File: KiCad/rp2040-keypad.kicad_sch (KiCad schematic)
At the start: 21 parts

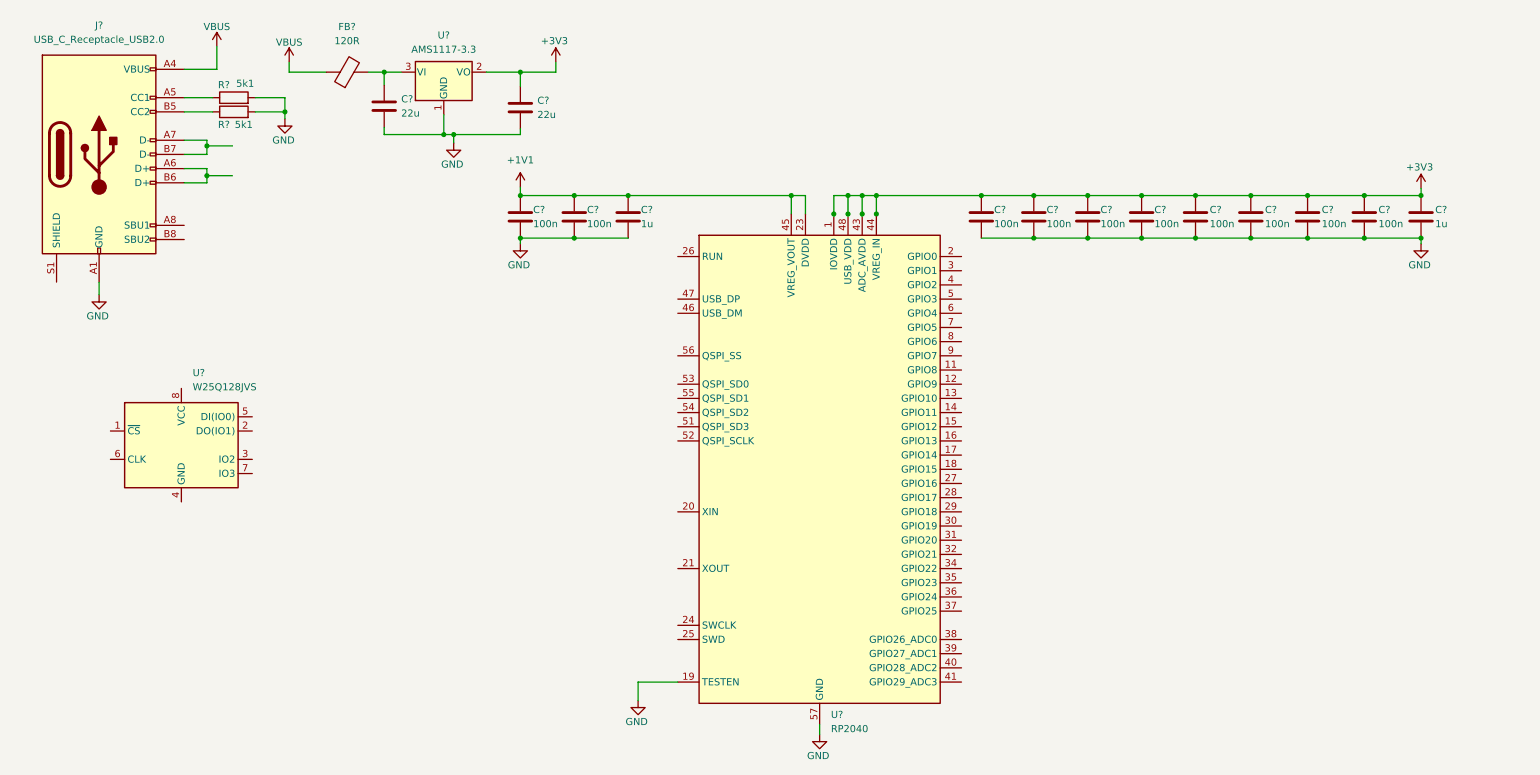
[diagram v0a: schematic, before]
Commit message: Finish schematic and footprint assignment
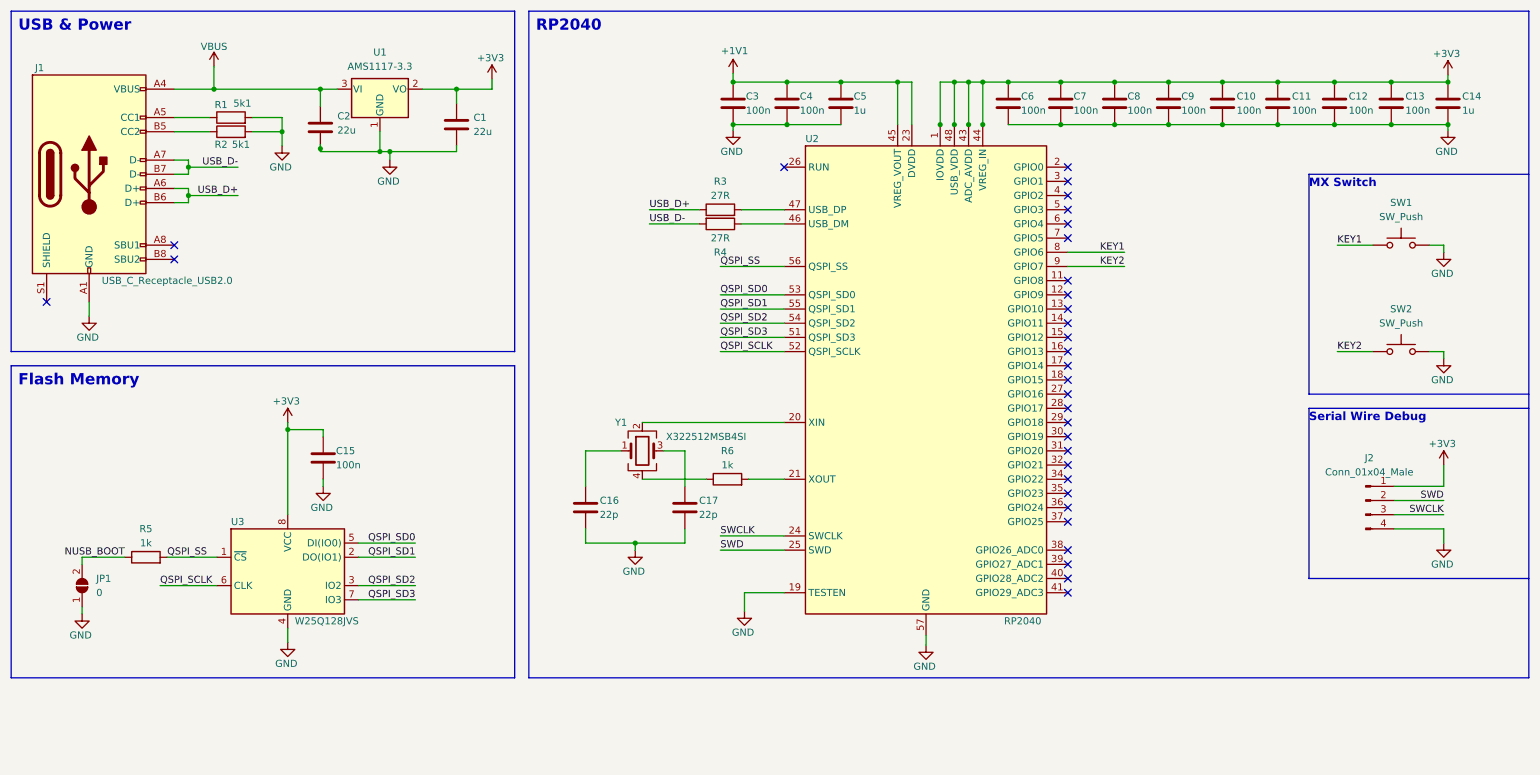
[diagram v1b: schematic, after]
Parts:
- removed FB?: 120R, symbol Device:FerriteBead
- added C15: 100n, Capacitor_SMD:C_0402_1005Metric, symbol Device:C
- added C16, C17: 22p, Capacitor_SMD:C_0402_1005Metric, symbol Device:C
- added J2: Conn_01x04_Male, Connector_Wire:SolderWire-0.1sqmm_1x04_P3.6mm_D0.4mm_OD1mm, symbol Connector:Conn_01x04_Male
- added JP1: 0, Jumper:SolderJumper-2_P1.3mm_Open_Pad1.0x1.5mm, symbol Jumper:SolderJumper_2_Open
- added R3, R4: 27R, Resistor_SMD:R_0402_1005Metric, symbol Device:R
- added R5, R6: 1k, Resistor_SMD:R_0402_1005Metric, symbol Device:R
- added SW1, SW2: SW_Push, Switch_Keyboard_Cherry_MX:SW_Cherry_MX_PCB_1.00u, symbol Switch:SW_Push
- added Y1: X322512MSB4SI, Crystal:Crystal_SMD_3225-4Pin_3.2x2.5mm, symbol Device:Crystal_GND24
- C1, C2: renamed from C?; footprint (none) -> Capacitor_SMD:C_0603_1608Metric
- C10, C11, C12, C13, C14, C3, C4, C5, C6, C7, C8, C9: renamed from C?; footprint (none) -> Capacitor_SMD:C_0402_1005Metric
- J1: renamed from J?; footprint (none) -> Connector_USB:USB_C_Receptacle_HRO_TYPE-C-31-M-12
- R1, R2: renamed from R?; footprint (none) -> Resistor_SMD:R_0402_1005Metric
- gave numbers to parts that had none: 3
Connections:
- net +3V3: now also U3.8 (VCC), C15.1, J2.1 (Pin_1)
- net GND: now also U3.4 (GND), C15.2, C16.2, C17.2, J2.4 (Pin_4), JP1.1 (A), SW1.2, SW2.2
- net VBUS: now also C2.1, U1.3 (VI)
- net at U2.20 (XIN): now also Y1.2
- net at U2.21 (XOUT): now also R6.2
- net SWCLK: now reaches U2.24 (SWCLK)
- net SWCLK: now also J2.3 (Pin_3)
- net SWD: now reaches U2.25 (SWD)
- net SWD: now also J2.2 (Pin_2)
- net at U2.46 (USB_DM): now also R4.1
- net at U2.47 (USB_DP): now also R3.2
- net QSPI_SD3: now reaches U2.51 (QSPI_SD3)
- net QSPI_SD3: now also U3.7 (IO3)
- net QSPI_SCLK: now reaches U2.52 (QSPI_SCLK)
- net QSPI_SCLK: now also U3.6 (CLK)
- net QSPI_SD0: now reaches U2.53 (QSPI_SD0)
- net QSPI_SD0: now also U3.5 (DI(IO0))
- net QSPI_SD2: now reaches U2.54 (QSPI_SD2)
- net QSPI_SD2: now also U3.3 (IO2)
- net QSPI_SD1: now reaches U2.55 (QSPI_SD1)
- net QSPI_SD1: now also U3.2 (DO(IO1))
- net QSPI_SS: now reaches U2.56 (QSPI_SS)
- net QSPI_SS: now also U3.1 (~{CS}), R5.2
- net KEY1: now reaches U2.8 (GPIO6)
- net KEY1: now also SW1.1
- net KEY2: now reaches U2.9 (GPIO7)
- net KEY2: now also SW2.1
- net USB_D+: now reaches J1.A6 (D+), J1.B6 (D+)
- net USB_D+: now also R3.1
- net USB_D-: now reaches J1.A7 (D-), J1.B7 (D-)
- net USB_D-: now also R4.2
- new net: C16.1, Y1.1
- new net: C17.1, Y1.3
- new net: R6.1, Y1.4
- new net NUSB_BOOT: JP1.2 (B), R5.1
- no-connect marks 0 -> 32
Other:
- note added: "Flash Memory"
- note added: "MX Switch"
- note added: "RP2040"
- note added: "Serial Wire Debug"
- note added: "USB & Power"
- moved on the sheet: C1, C10, C11, C12, C13, C14, C2, C3, C4, C5, C6, C7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

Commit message: First draft completed ready to review
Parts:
- added H1, H2, H3, H4: MountingHole, MountingHole:MountingHole_2.2mm_M2_DIN965, symbol Mechanical:MountingHole
- C1, C2: LCSC (none) -> C59461
- C10, C11, C12, C13, C15, C3, C4, C6, C7, C8, C9: LCSC (none) -> C1525
- C14, C5: LCSC (none) -> C52923
- C16, C17: LCSC (none) -> C1555
- J1: LCSC (none) -> C165948
- R1, R2: LCSC (none) -> C25905
- R3, R4: value 27R -> 27R4; LCSC (none) -> C26971
- R5, R6: LCSC (none) -> C11702
- U1: LCSC (none) -> C6186
- U2: LCSC (none) -> C2040
- U3: LCSC (none) -> C97521
- Y1: value X322512MSB4SI -> 12Mhz; LCSC (none) -> C9002
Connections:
- net GND: now also Y1.2, Y1.4
- net at Y1.1: now also C17.1, R6.1; no longer C16.1
- net at U2.20 (XIN): now also C16.1, Y1.3; no longer Y1.2
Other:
- moved on the sheet: Y1

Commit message: Rev 0.1 ready for production
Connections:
- net D-: now reaches R4.1, U2.46 (USB_DM)
- net D+: now reaches R3.2, U2.47 (USB_DP)
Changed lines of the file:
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@@
     (effects (font (size 1.27 1.27)) (justify right bottom))
+  )
+  (label "D+" (at 147.32 48.26 0)
+    (effects (font (size 1.27 1.27)) (justify left bottom))
   )
   (label "SWD" (at 269.24 100.33 180)
@@
     (effects (font (size 1.27 1.27)) (justify left bottom))
   )
+  (label "D-" (at 147.32 50.8 0)
+    (effects (font (size 1.27 1.27)) (justify left bottom))
+  )

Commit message: Fix component ID R3&R4 for JLCPCB
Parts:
- R3, R4: LCSC C26971 -> C31439
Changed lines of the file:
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@@
       (effects (font (size 1.27 1.27)) hide)
     )
-    (property "LCSC" "C26971" (id 4) (at 139.7 50.8 90)
+    (property "LCSC" "C31439" (id 4) (at 139.7 50.8 90)
       (effects (font (size 1.27 1.27)) hide)
     )
@@
       (effects (font (size 1.27 1.27)) hide)
     )
-    (property "LCSC" "C26971" (id 4) (at 139.7 48.26 90)
-      (effects (font (size 1.27 1.27)) hide)
-    )
+    (property "LCSC" "C31439" (id 4) (at 139.7 48.26 90)
+      (effects (font (size 1.27 1.27)) hide)
+    )
